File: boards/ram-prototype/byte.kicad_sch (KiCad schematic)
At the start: 48 parts, among them U1 74LVC1G79, U10 74LVC1G125, U11 74LVC1G79, U12 74LVC1G125, U13 74LVC1G79, U14 74LVC1G125, U15 74LVC1G79, U16 74LVC1G125, U2 74LVC1G125, U3 74LVC1G79, U4 74LVC1G125, U5 74LVC1G79, U6 74LVC1G125, U7 74LVC1G79, U8 74LVC1G125, U9 74LVC1G79

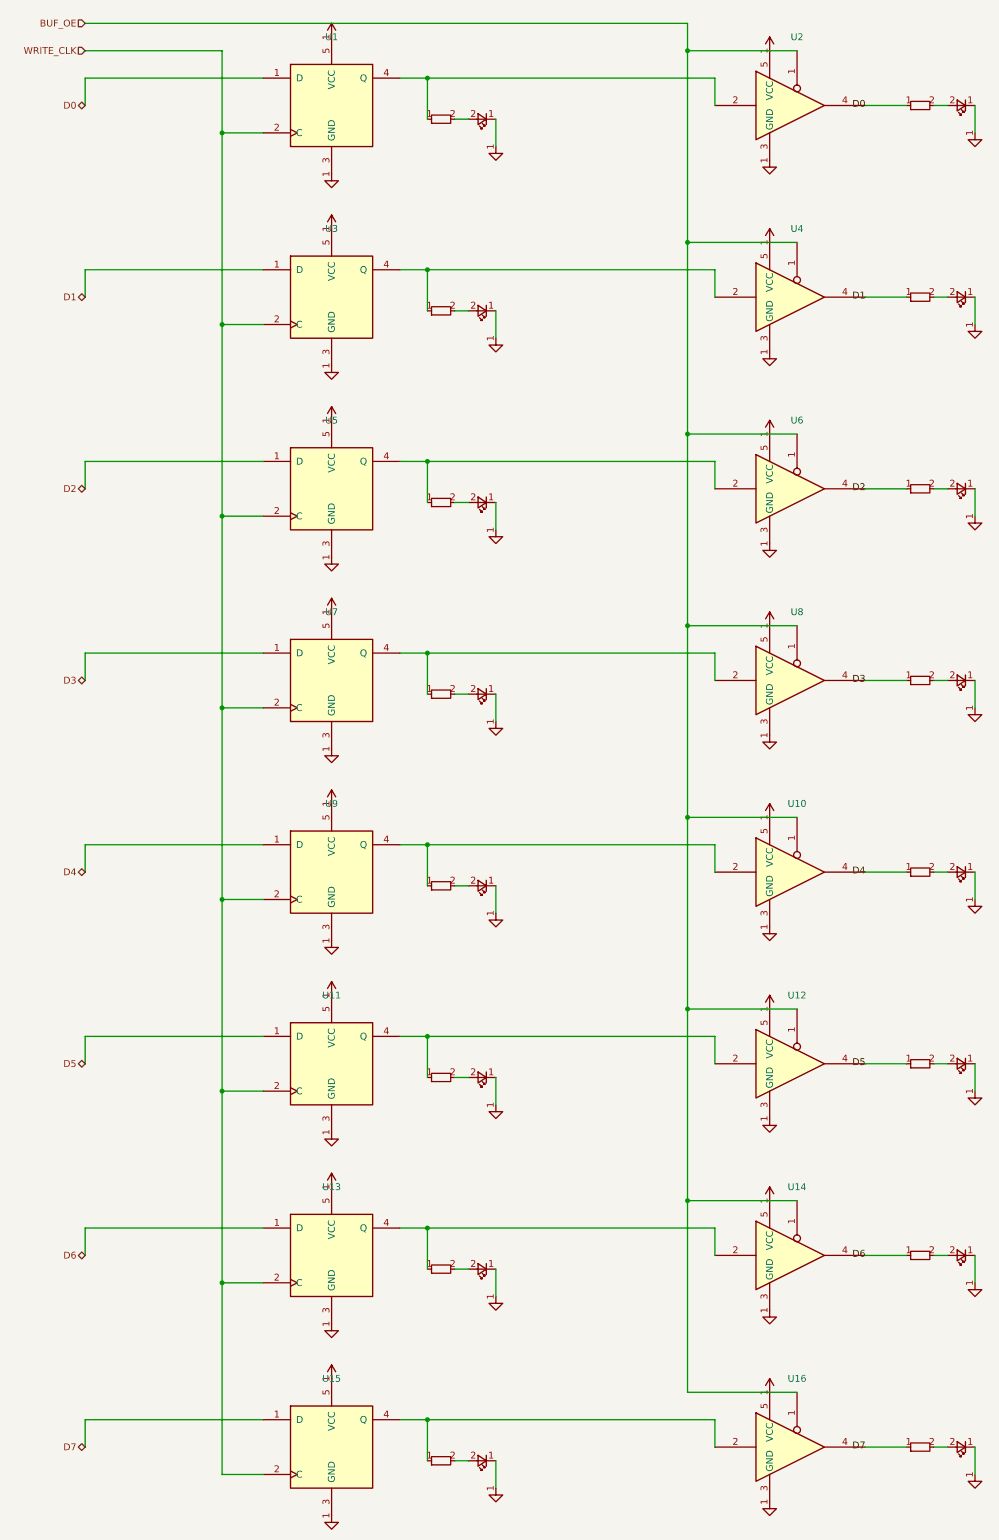
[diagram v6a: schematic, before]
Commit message: add and fix some checks
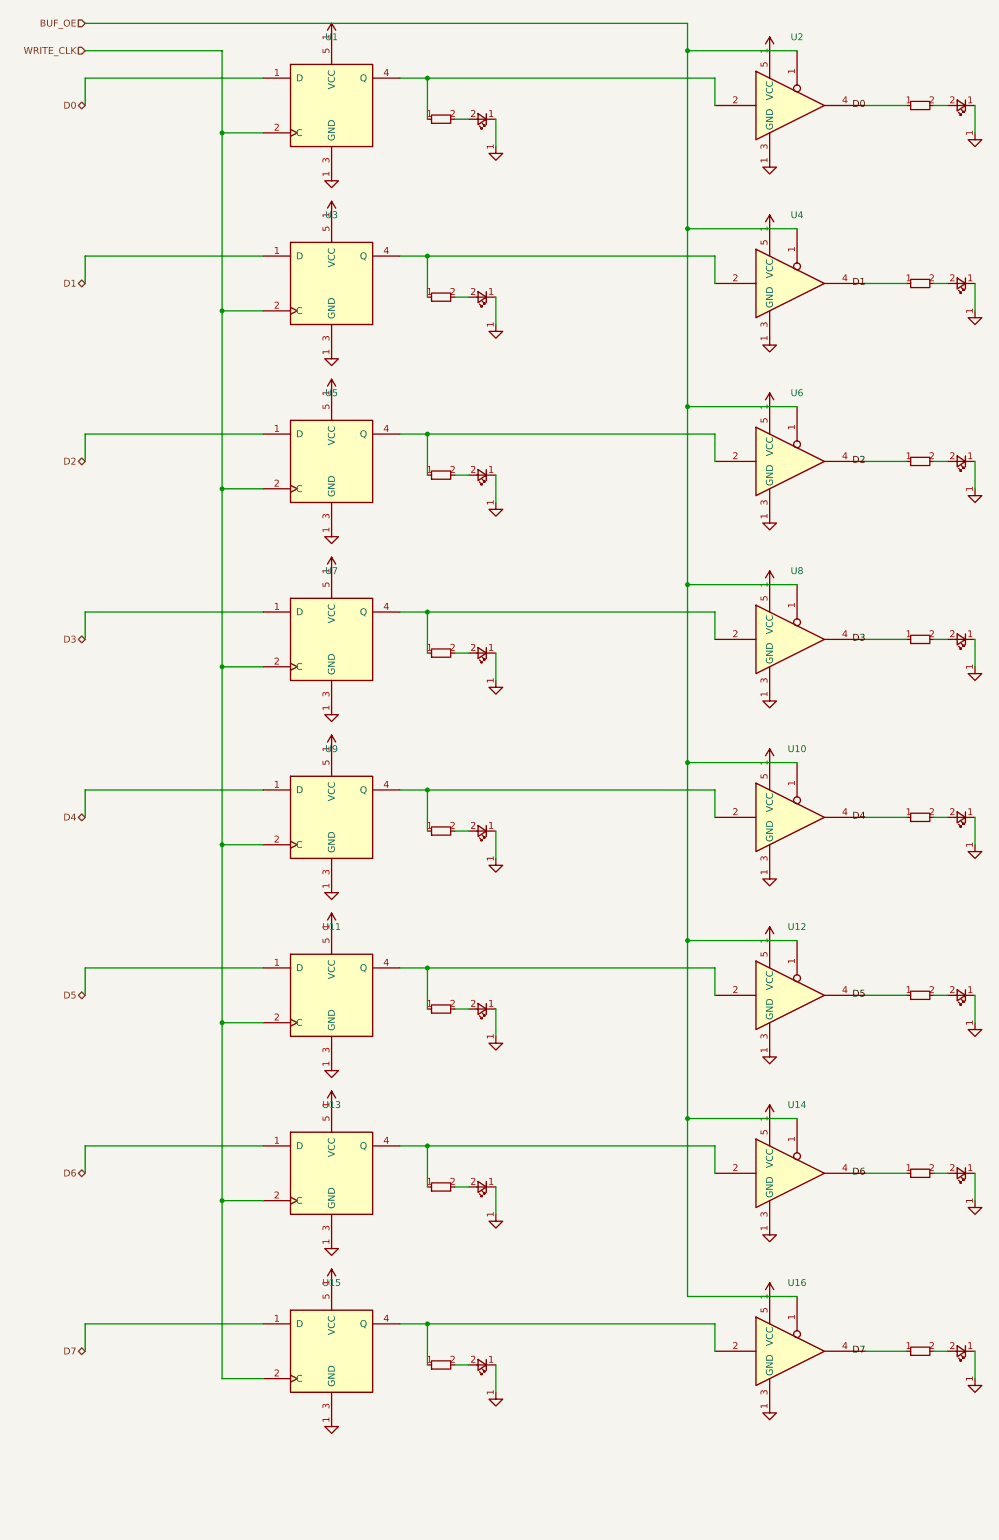
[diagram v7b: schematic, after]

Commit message: Fix labelling
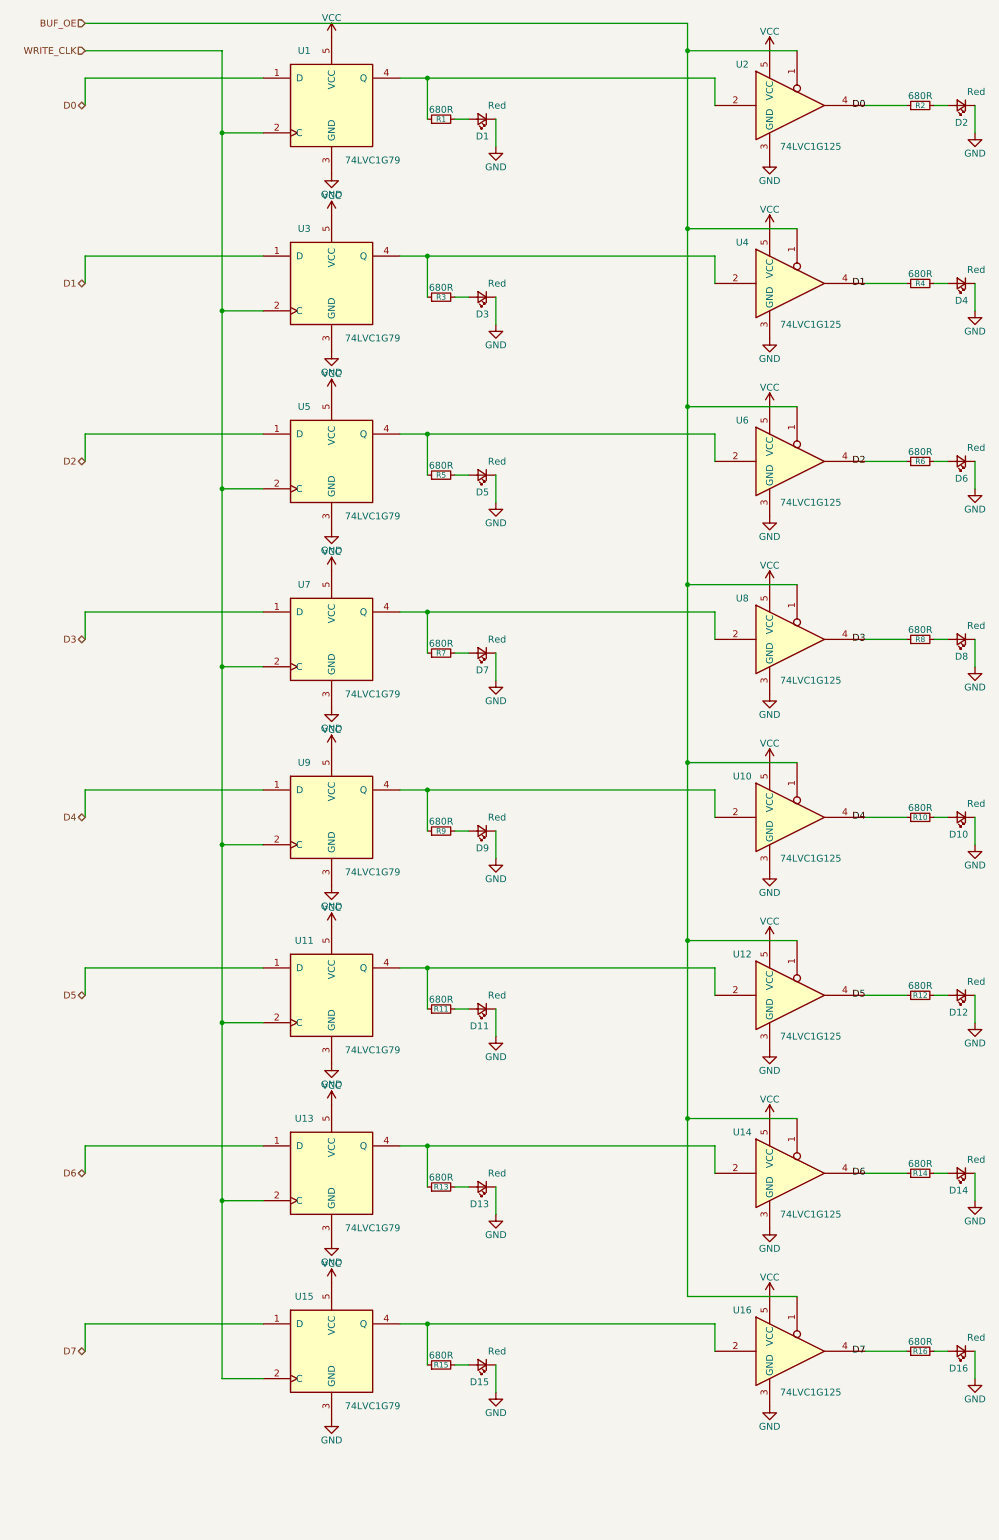
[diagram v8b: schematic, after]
